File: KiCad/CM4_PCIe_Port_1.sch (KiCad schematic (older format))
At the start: 1 part, among them J14 PCIe_x16

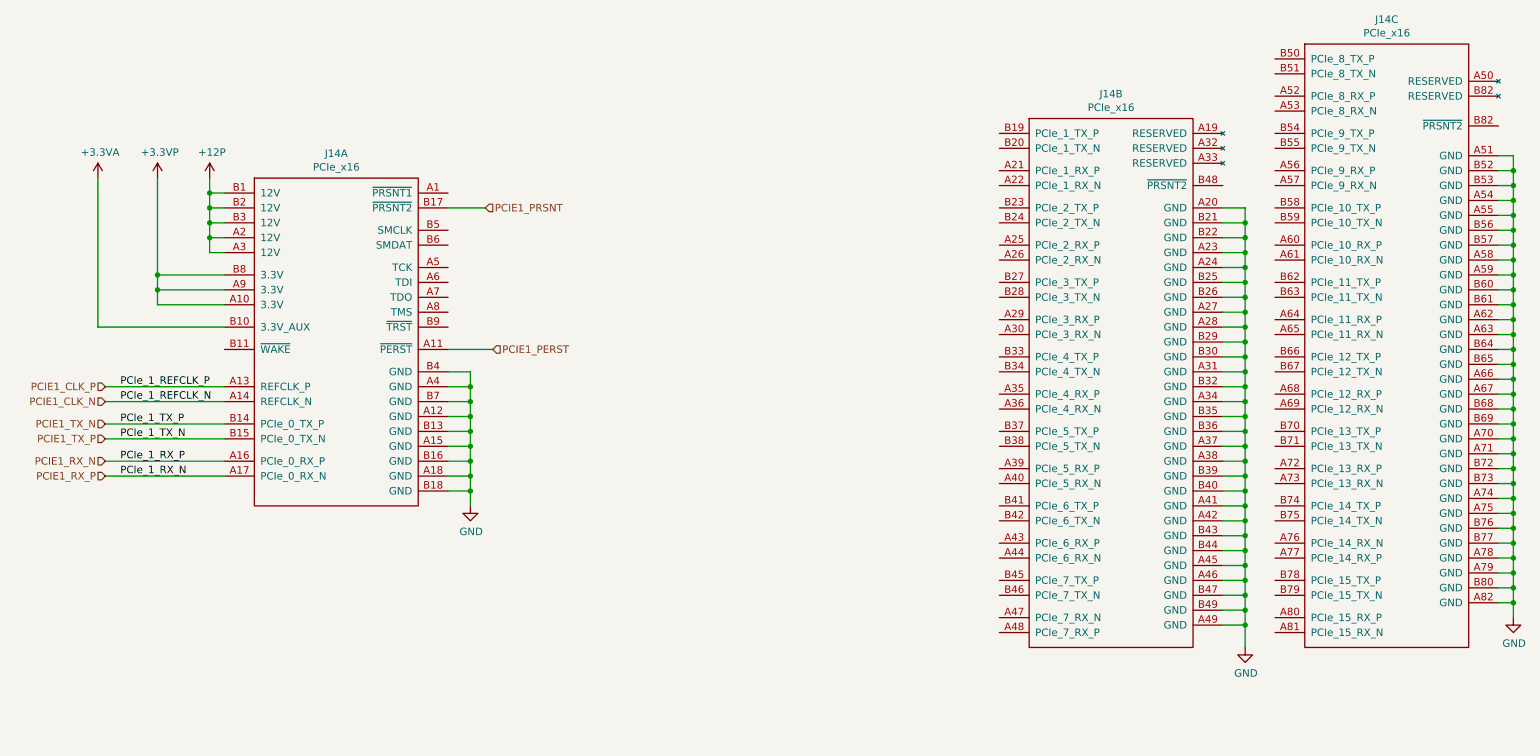
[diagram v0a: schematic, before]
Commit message: Adding PCIe subsystem
- Moves a lot of the PCIe related items from the top level sheet to a new sheet called PCIe Subsystem which then has other hierarchical sheets below it.

- This adds some of the AC coupling caps for the PCIe slots, might need to do some work with the switch yet.

- Adds an SMBUS mux for the SMBUS connections to the PCIe slots. Extra SMBUS lanes sit un-wired and can be used for other things.

- Adds JTAG headers for the PCIe connectors.
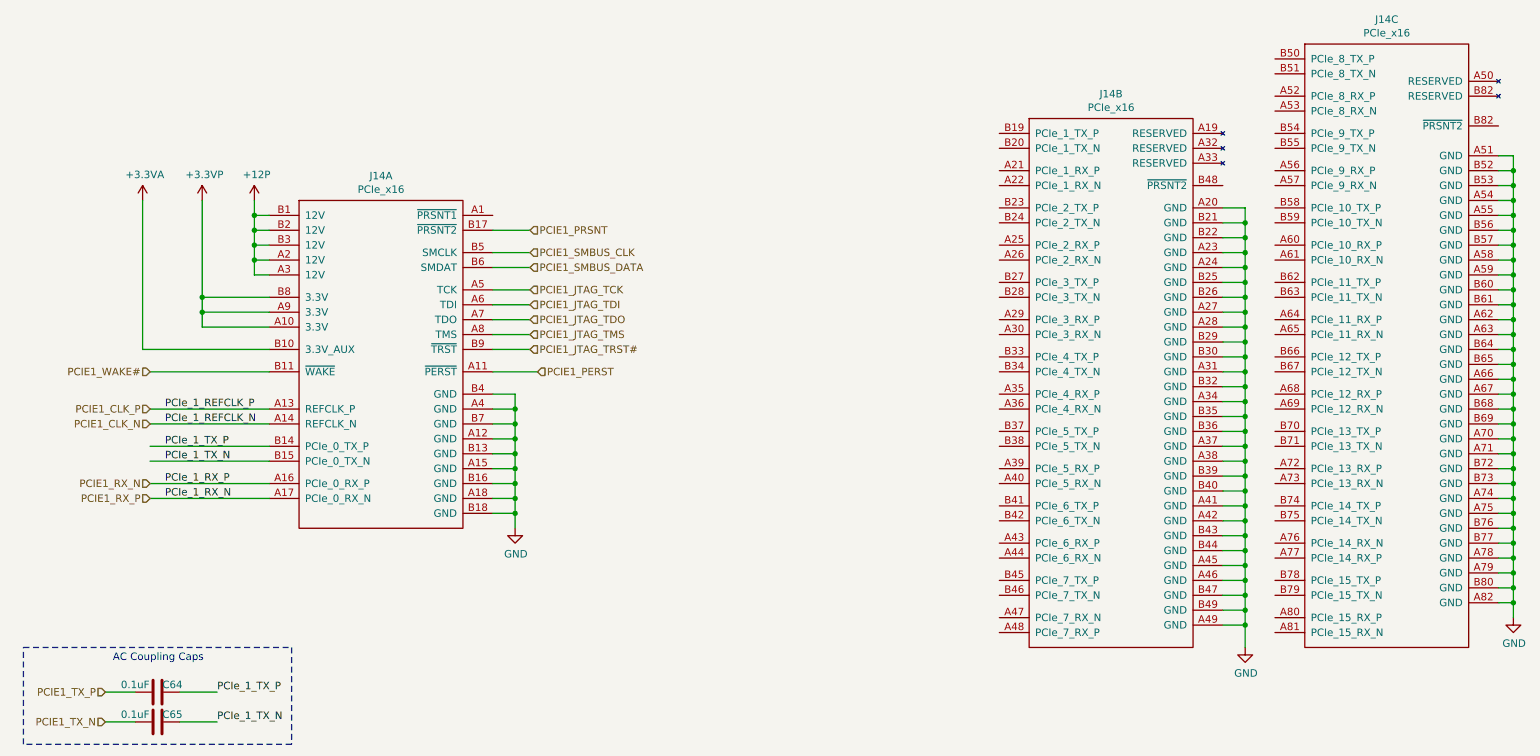
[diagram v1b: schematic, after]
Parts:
- added C64, C65: 0.1uF, symbol CM4_MATX:C
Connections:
- net PCIE1_TX_N: now also C65.2; no longer J14.B14 (PCIe_0_TX_P)
- net PCIE1_TX_P: now also C64.1; no longer J14.B15 (PCIe_0_TX_N)
- net PCIE1_JTAG_TCK: now reaches J14.A5 (TCK)
- net PCIE1_JTAG_TDI: now reaches J14.A6 (TDI)
- net PCIE1_JTAG_TDO: now reaches J14.A7 (TDO)
- net PCIE1_JTAG_TMS: now reaches J14.A8 (TMS)
- net PCIE1_WAKE#: now reaches J14.B11 (~WAKE)
- net PCIE1_SMBUS_CLK: now reaches J14.B5 (SMCLK)
- net PCIE1_SMBUS_DATA: now reaches J14.B6 (SMDAT)
- net PCIE1_JTAG_TRST#: now reaches J14.B9 (~TRST)
- new net PCIe_1_TX_N: C65.1, J14.B15 (PCIe_0_TX_N)
- new net PCIe_1_TX_P: C64.2, J14.B14 (PCIe_0_TX_P)
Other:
- note added: "AC Coupling Caps"
- moved on the sheet: J14A
